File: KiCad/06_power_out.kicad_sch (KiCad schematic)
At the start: 0 parts

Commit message: First scheme complete
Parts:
- added D601, D602, D603, D604, D605, D606: LED, LED_SMD:LED_0603_1608Metric, symbol Device:LED
- added J601, J602: Conn_02x03_Odd_Even, Connector_PinHeader_2.54mm:PinHeader_2x03_P2.54mm_Vertical, symbol Connector_Generic:Conn_02x03_Odd_Even
- added R601, R602, R603, R604, R605, R606: 510R, Resistor_SMD:R_0402_1005Metric, symbol Device:R
- added S601, S602, S603: XKB5858-Z, psu:XKB5858Z, symbol psu:XKB5858-Z
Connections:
- new net: D601.2 (A), R601.1
- new net: D605.2 (A), R605.1
- new net: D606.1 (K), S603.6
- new net: D606.2 (A), R606.1
- new net: D603.2 (A), R603.1
- new net: D604.2 (A), R604.1
- new net: D601.1 (K), S601.4
- new net: D602.1 (K), S601.6
- new net: D604.1 (K), S602.6
- new net: D602.2 (A), R602.1
- new net: D605.1 (K), S603.4
- new net: D603.1 (K), S602.4
- new net +3V3: S601.3, S602.3
- new net +3V3_FTDI: S603.3
- new net +5V: S601.1, S602.1
- new net +VCC_USB2UART_FILT: R605.2, R606.2, S603.1
- new net +VIN_SWITCH: R601.2, R602.2, R603.2, R604.2
- new net GND: J601.2 (Pin_2), J601.4 (Pin_4), J601.6 (Pin_6), J602.2 (Pin_2), J602.4 (Pin_4), J602.6 (Pin_6), S601.5, S602.5, S603.5
- new net VCC_FTDI: S603.2
- new net VCC_L: J601.1 (Pin_1), J601.3 (Pin_3), J601.5 (Pin_5), S601.2
- new net VCC_R: J602.1 (Pin_1), J602.3 (Pin_3), J602.5 (Pin_5), S602.2
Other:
- note added: "FTDI power switch"
- note added: "Left power switch"
- note added: "Right power switch"

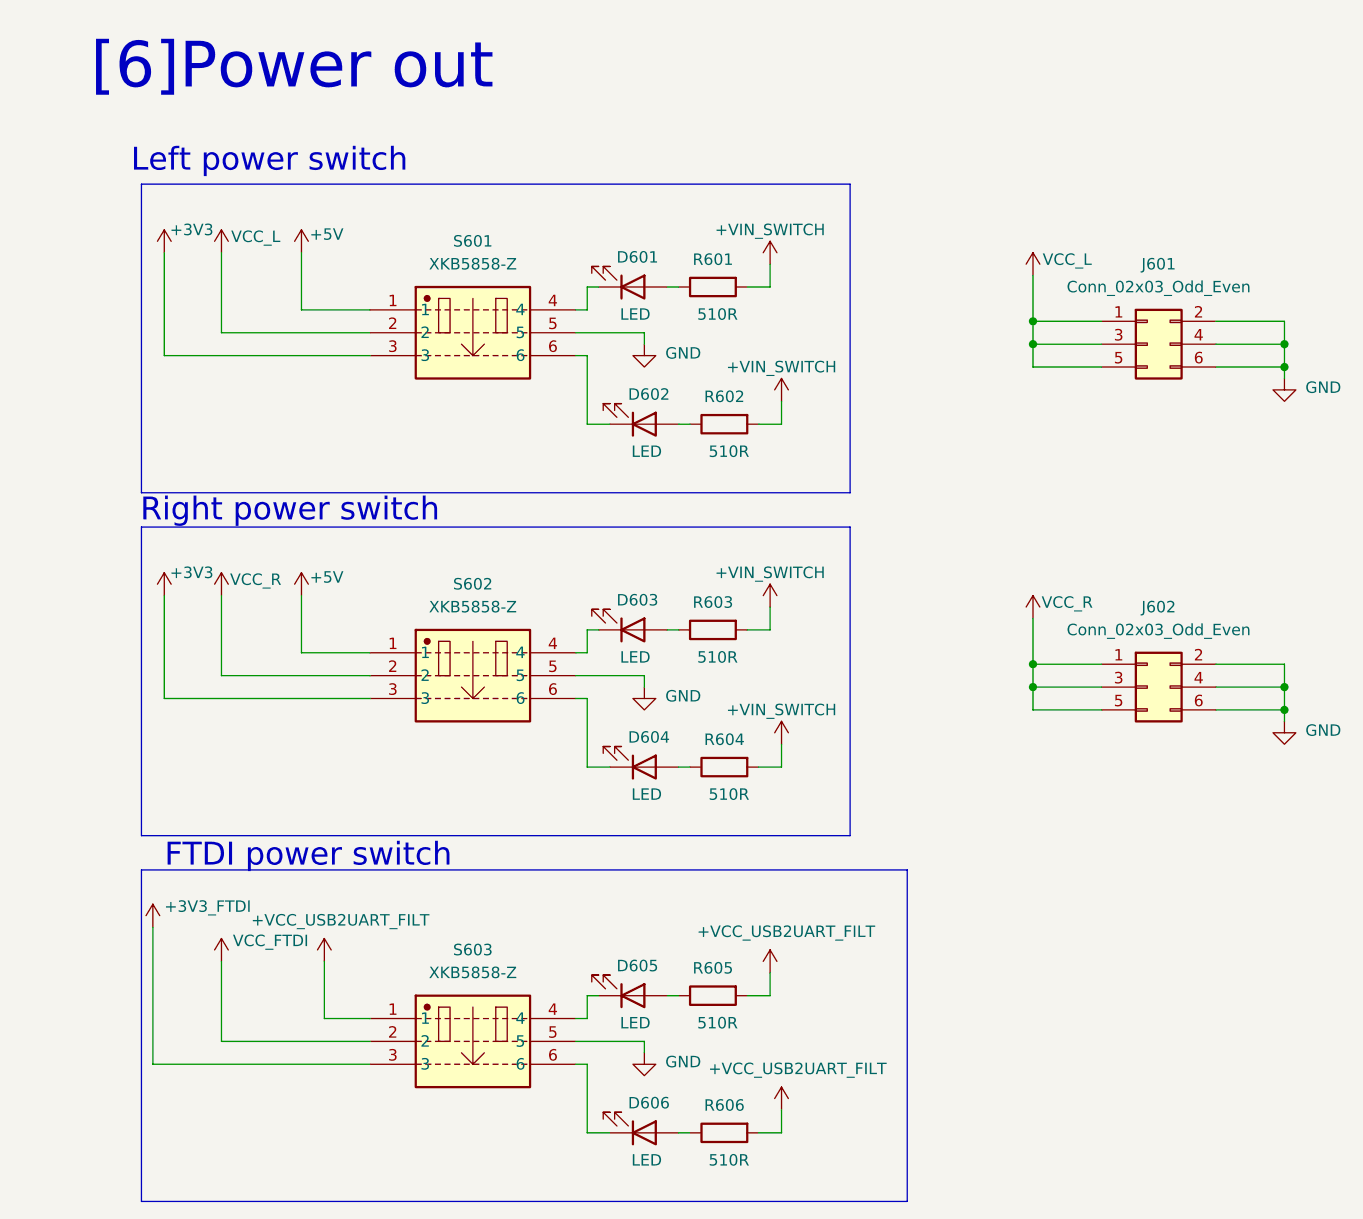
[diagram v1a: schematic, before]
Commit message: Add power out capacitors
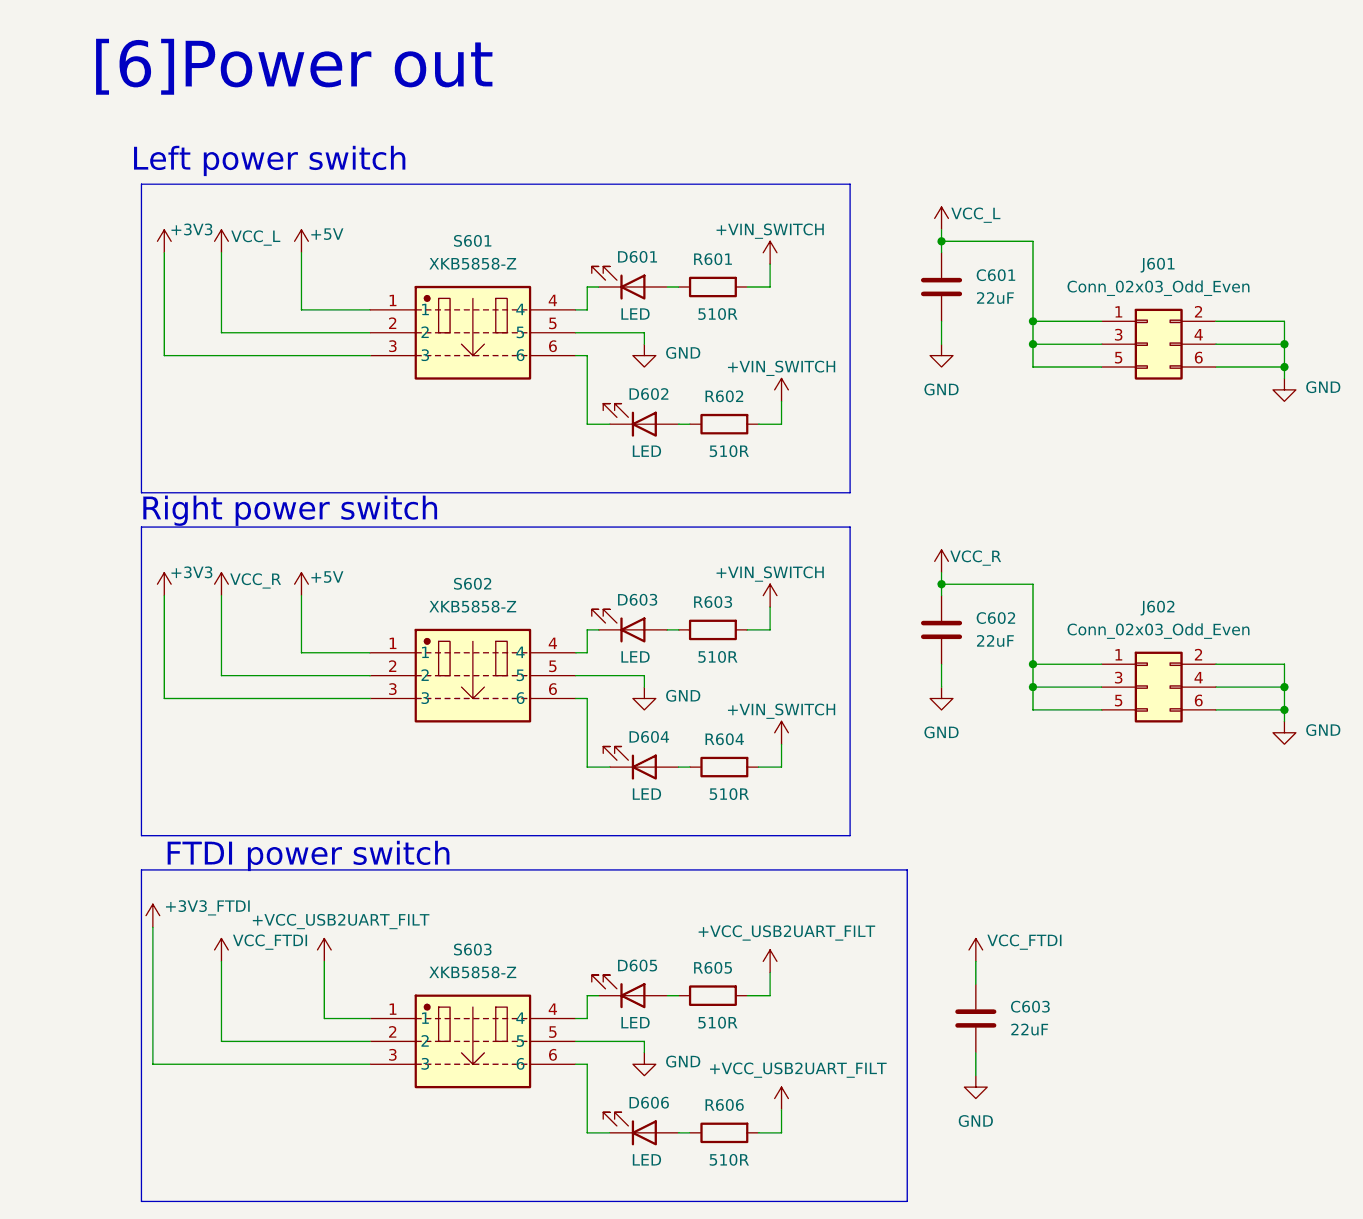
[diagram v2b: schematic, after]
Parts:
- added C601, C602, C603: 22uF, Capacitor_SMD:C_0805_2012Metric, symbol Device:C
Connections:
- net GND: now also C601.2, C602.2, C603.2
- net VCC_FTDI: now also C603.1
- net VCC_L: now also C601.1
- net VCC_R: now also C602.1

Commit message: ERC fixes
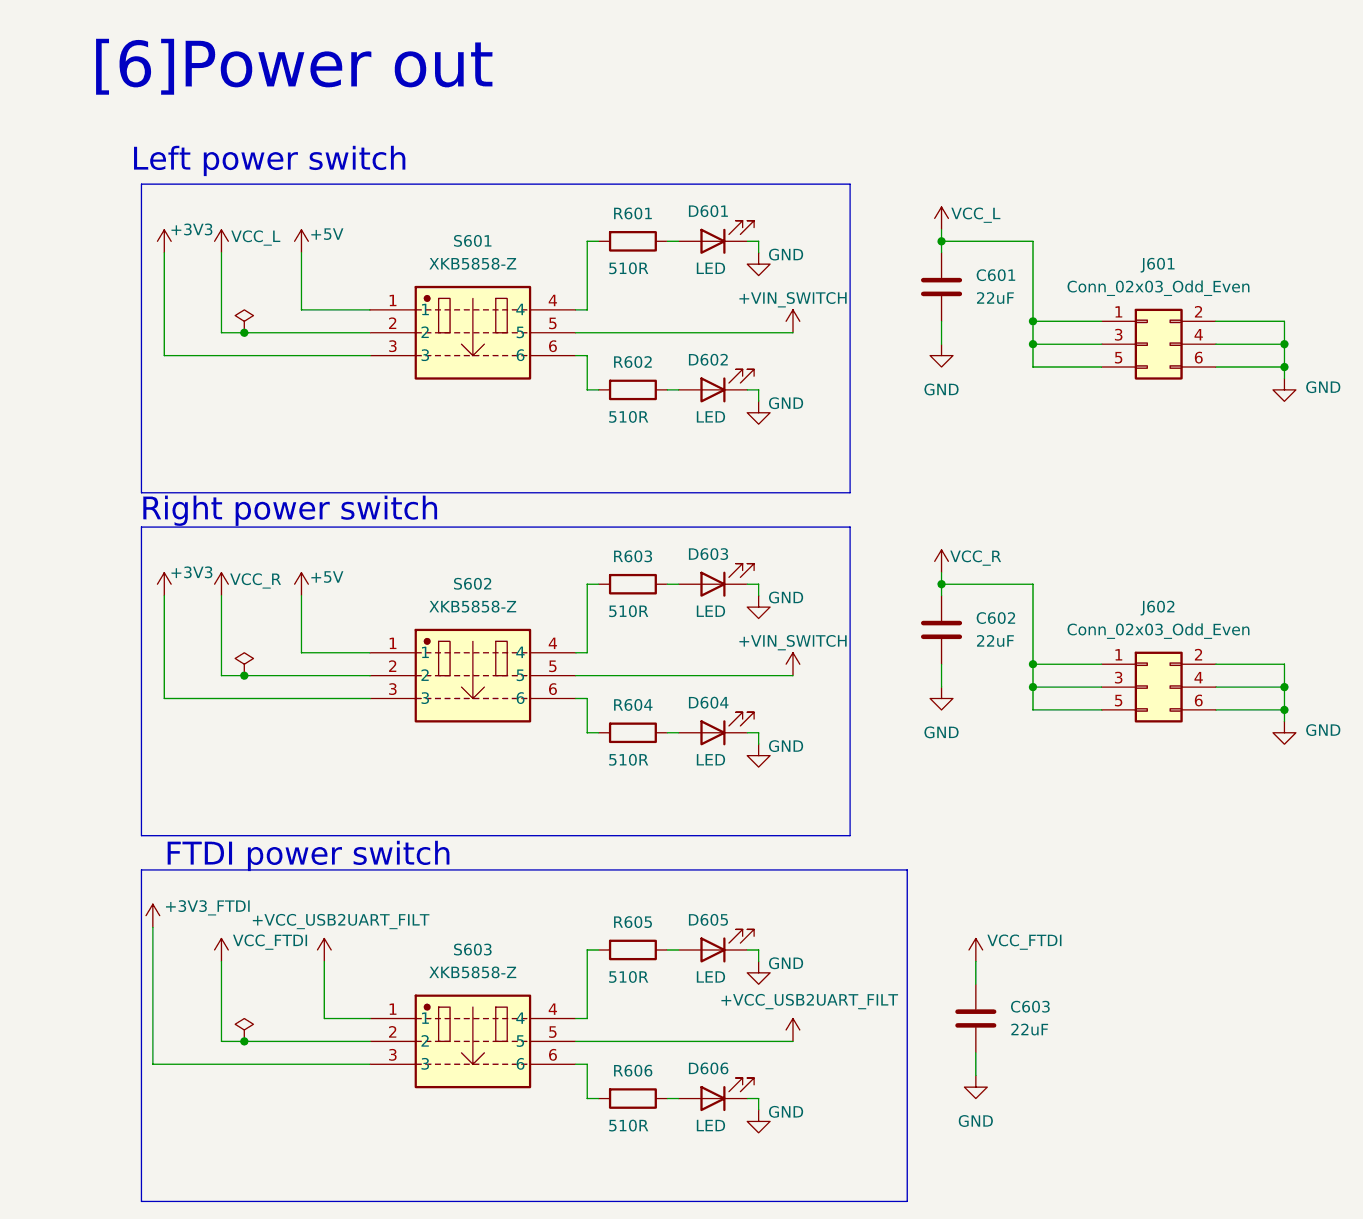
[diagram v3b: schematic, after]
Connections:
- net +VCC_USB2UART_FILT: now also S603.5; no longer R605.2, R606.2
- net +VIN_SWITCH: now also S601.5, S602.5; no longer R601.2, R602.2, R603.2, R604.2
- net GND: now also D601.1 (K), D602.1 (K), D603.1 (K), D604.1 (K), D605.1 (K), D606.1 (K); no longer S601.5, S602.5, S603.5
- net at S603.6: now also R606.2; no longer D606.1 (K)
- net at S601.4: now also R601.2; no longer D601.1 (K)
- net at S601.6: now also R602.2; no longer D602.1 (K)
- net at S602.6: now also R604.2; no longer D604.1 (K)
- net at S603.4: now also R605.2; no longer D605.1 (K)
- net at S602.4: now also R603.2; no longer D603.1 (K)
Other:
- moved on the sheet: D601, R601

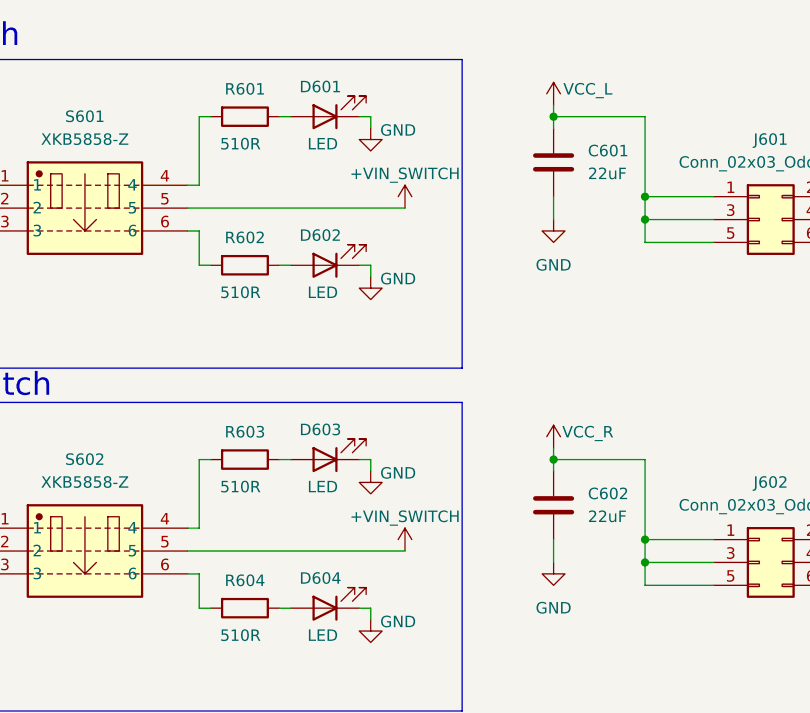
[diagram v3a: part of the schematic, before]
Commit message: battery connector PCB routing
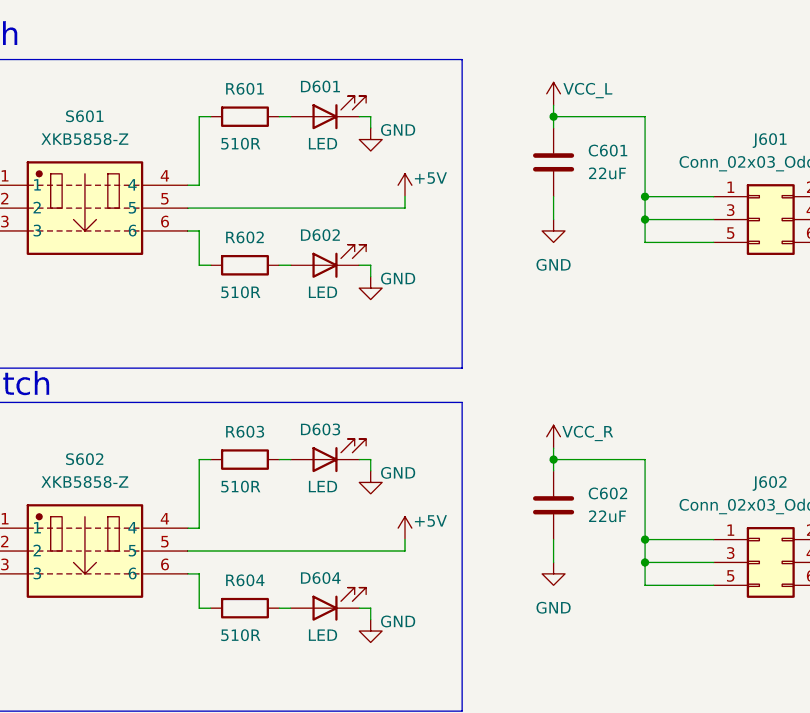
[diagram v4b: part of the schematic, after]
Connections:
- net +VIN_SWITCH is gone; now on net +5V: S601.5, S602.5
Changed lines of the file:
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@@
 	(wire
 		(pts
+			(xy 95.25 86.36) (xy 95.25 87.63)
+		)
+		(stroke
+			(width 0)
+			(type default)
+		)
+	)
+	(wire
+		(pts
 			(xy 72.39 77.47) (xy 73.66 77.47)
 		)
@@
 	(wire
 		(pts
+			(xy 95.25 48.26) (xy 95.25 49.53)
+		)
+		(stroke
+			(width 0)
+			(type default)
+		)
+	)
+	(wire
+		(pts
 			(xy 71.12 125.73) (xy 72.39 125.73)
 		)
@@
 	)
 	(symbol
+		(lib_id "power:+3.3V")
+		(at 95.25 86.36 0)
+		(unit 1)
+		(exclude_from_sim no)
+		(in_bom yes)
+		(on_board yes)
+		(dnp no)
+		(property "Reference" "#PWR0615"
+			(at 95.25 90.17 0)
+			(effects
+				(font
+					(size 1.27 1.27)
+				)
+				(hide yes)
+			)
+		)
+		(property "Value" "+5V"
+			(at 98.044 84.328 0)
+			(effects
+				(font
+					(size 1.27 1.27)
+				)
+			)
+		)
+		(property "Footprint" ""
+			(at 95.25 86.36 0)
+			(effects
+				(font
+					(size 1.27 1.27)
+				)
+				(hide yes)
+			)
+		)
+		(property "Datasheet" ""
+			(at 95.25 86.36 0)
+			(effects
+				(font
+					(size 1.27 1.27)
+				)
+				(hide yes)
+			)
+		)
+		(property "Description" "Power symbol creates a global label with name \"+5V\""
+			(at 95.25 86.36 0)
+			(effects
+				(font
+					(size 1.27 1.27)
+				)
+				(hide yes)
+			)
+		)
+		(pin "1"
+		)
+		(instances
+			(project "solderless_breadboard_psu"
+				(path "/daadd221-9750-45f3-8ee2-46422755319d/fb884ed1-1487-4429-a624-834d1e55909d"
+					(reference "#PWR0615")
+					(unit 1)
+				)
+			)
+		)
+	)
+	(symbol
 		(lib_id "Device:R")
 		(at 77.47 39.37 270)
@@
 	(symbol
 		(lib_id "power:+3.3V")
+		(at 95.25 48.26 0)
+		(unit 1)
+		(exclude_from_sim no)
+		(in_bom yes)
+		(on_board yes)
+		(dnp no)
+		(property "Reference" "#PWR0606"
+			(at 95.25 52.07 0)
+			(effects
+				(font
+					(size 1.27 1.27)
+				)
+				(hide yes)
+			)
+		)
+		(property "Value" "+5V"
+			(at 98.044 46.228 0)
+			(effects
+				(font
+					(size 1.27 1.27)
+				)
+			)
+		)
+		(property "Footprint" ""
+			(at 95.25 48.26 0)
+			(effects
+				(font
+					(size 1.27 1.27)
+				)
+				(hide yes)
+			)
+		)
+		(property "Datasheet" ""
+			(at 95.25 48.26 0)
+			(effects
+				(font
+					(size 1.27 1.27)
+				)
+				(hide yes)
+			)
+		)
+		(property "Description" "Power symbol creates a global label with name \"+5V\""
+			(at 95.25 48.26 0)
+			(effects
+				(font
+					(size 1.27 1.27)
+				)
+				(hide yes)
+			)
+		)
+		(pin "1"
+		)
+		(instances
+			(project "solderless_breadboard_psu"
+				(path "/daadd221-9750-45f3-8ee2-46422755319d/fb884ed1-1487-4429-a624-834d1e55909d"
+					(reference "#PWR0606")
+					(unit 1)
+				)
+			)
+		)
+	)
+	(symbol
+		(lib_id "power:+3.3V")
 		(at 25.4 78.74 0)
 		(unit 1)
@@
 	)
 	(symbol
-		(lib_id "power:+5V")
-		(at 95.25 87.63 0)
-		(unit 1)
-		(exclude_from_sim no)
-		(in_bom yes)
-		(on_board yes)
-		(dnp no)
-		(property "Reference" "#PWR0615"
-			(at 95.25 91.44 0)
-			(effects
-				(font
-					(size 1.27 1.27)
-				)
-				(hide yes)
-			)
-		)
-		(property "Value" "+VIN_SWITCH"
-			(at 95.25 83.82 0)
-			(effects
-				(font
-					(size 1.27 1.27)
-				)
-			)
-		)
-		(property "Footprint" ""
-			(at 95.25 87.63 0)
-			(effects
-				(font
-					(size 1.27 1.27)
-				)
-				(hide yes)
-			)
-		)
-		(property "Datasheet" ""
-			(at 95.25 87.63 0)
-			(effects
-				(font
-					(size 1.27 1.27)
-				)
-				(hide yes)
-			)
-		)
-		(property "Description" ""
-			(at 95.25 87.63 0)
-			(effects
-				(font
-					(size 1.27 1.27)
-				)
-				(hide yes)
-			)
-		)
-		(pin "1"
-		)
-		(instances
-			(project "solderless_breadboard_psu"
-				(path "/daadd221-9750-45f3-8ee2-46422755319d/fb884ed1-1487-4429-a624-834d1e55909d"
-					(reference "#PWR0615")
-					(unit 1)
-				)
-			)
-		)
-	)
-	(symbol
 		(lib_id "Device:R")
 		(at 77.47 134.62 270)
@@
 					(unit 1)
 				)
-			)
-		)
-	)
-	(symbol
-		(lib_id "power:+5V")
-		(at 95.25 49.53 0)
-		(unit 1)
-		(exclude_from_sim no)
-		(in_bom yes)
-		(on_board yes)
-		(dnp no)
-		(property "Reference" "#PWR0606"
-			(at 95.25 53.34 0)
-			(effects
-				(font
-					(size 1.27 1.27)
-				)
-				(hide yes)
-			)
-		)
-		(property "Value" "+VIN_SWITCH"
-			(at 95.25 45.72 0)
-			(effects
-				(font
-					(size 1.27 1.27)
-				)
-			)
-		)
-		(property "Footprint" ""
-			(at 95.25 49.53 0)
-			(effects
-				(font
-					(size 1.27 1.27)
-				)
-				(hide yes)
-			)
-		)
-		(property "Datasheet" ""
-			(at 95.25 49.53 0)
-			(effects
-				(font
-					(size 1.27 1.27)
-				)
-				(hide yes)
-			)
-		)
-		(property "Description" ""
-			(at 95.25 49.53 0)
-			(effects
-				(font
-					(size 1.27 1.27)
-				)
-				(hide yes)
-			)
-		)
-		(pin "1"
-		)
-		(instances
-			(project "solderless_breadboard_psu"
-				(path "/daadd221-9750-45f3-8ee2-46422755319d/fb884ed1-1487-4429-a624-834d1e55909d"
-					(reference "#PWR0606")
-					(unit 1)
-				)
